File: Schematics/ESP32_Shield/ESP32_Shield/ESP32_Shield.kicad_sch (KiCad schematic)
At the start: 18 parts, among them J1 Conn_01x10, Q3 Si2319CDS, Q4 Si2319CDS, U6 ADS1234IPW, U7 SHT30-DIS

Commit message: kek
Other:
- note added: "-Verzerrung Spannungsteiler durch ADC Innenwiderstanding -> Widerstand verkleinen wenn nötig -Anti Aliasing -> Für DC? -Bestehende IC anschauen -> Nicht verfolgt. -wofür pullup -0.150s ladezeit überprüfen"
- note removed: "-Verzerrung Spannungsteiler durch ADC Innenwiderstanding -> Widerstand verkleinen wenn nötig -Anti Aliasing -> Für DC? -Bestehende IC anschauen -> Nicht verfolgt."
- moved on the sheet: Q4
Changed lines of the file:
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@@
 		)
 	)
-	(text "-Verzerrung Spannungsteiler durch ADC Innenwiderstanding -> Widerstand verkleinen wenn nötig\n-Anti Aliasing -> Für DC?\n-Bestehende IC anschauen -> Nicht verfolgt.\n\n"
+	(text "-Verzerrung Spannungsteiler durch ADC Innenwiderstanding -> Widerstand verkleinen wenn nötig\n-Anti Aliasing -> Für DC?\n-Bestehende IC anschauen -> Nicht verfolgt.\n-wofür pullup\n-0.150s ladezeit überprüfen\n\n"
 		(exclude_from_sim no)
 		(at 17.018 187.198 0)
@@
 	)
 	(junction
-		(at 209.55 140.97)
-		(diameter 0)
-		(color 0 0 0 0)
-	)
-	(junction
 		(at 234.95 149.86)
 		(diameter 0)
@@
 	(wire
 		(pts
-			(xy 190.5 153.67) (xy 209.55 153.67)
-		)
-		(stroke
-			(width 0)
-			(type default)
-		)
-	)
-	(wire
-		(pts
 			(xy 210.82 134.62) (xy 217.17 134.62)
 		)
@@
 	(wire
 		(pts
+			(xy 200.66 73.66) (xy 200.66 81.28)
+		)
+		(stroke
+			(width 0)
+			(type default)
+		)
+	)
+	(wire
+		(pts
 			(xy 76.2 34.29) (xy 91.44 34.29)
 		)
@@
 	(wire
 		(pts
-			(xy 180.34 144.78) (xy 185.42 144.78)
+			(xy 189.865 69.215) (xy 189.865 68.58)
 		)
 		(stroke
@@
 	(wire
 		(pts
-			(xy 209.55 129.54) (xy 209.55 140.97)
-		)
-		(stroke
-			(width 0)
-			(type default)
-		)
-	)
-	(wire
-		(pts
 			(xy 26.67 165.1) (xy 29.21 165.1)
 		)
@@
 	(wire
 		(pts
-			(xy 209.55 140.97) (xy 209.55 153.67)
+			(xy 209.55 140.97) (xy 209.55 129.54)
 		)
 		(stroke
@@
 	(wire
 		(pts
-			(xy 185.42 144.78) (xy 185.42 146.05)
+			(xy 189.865 68.58) (xy 193.04 68.58)
 		)
 		(stroke
@@
 	(global_label "!EN_DMS"
 		(shape input)
-		(at 180.34 144.78 180)
+		(at 189.865 69.215 180)
 		(fields_autoplaced yes)
 		(effects
@@
 		)
 		(property "Intersheetrefs" "${INTERSHEET_REFS}"
-			(at 169.372 144.78 0)
+			(at 178.897 69.215 0)
 			(effects
 				(font
@@
 	(symbol
 		(lib_id "power:+3.3V")
-		(at 180.34 153.67 90)
-		(mirror x)
+		(at 200.66 63.5 0)
 		(unit 1)
 		(exclude_from_sim no)
@@
 		(dnp no)
 		(property "Reference" "#PWR046"
-			(at 184.15 153.67 0)
+			(at 200.66 67.31 0)
 			(effects
 				(font
@@
 		)
 		(property "Value" "+3.3V"
-			(at 175.26 153.67 90)
+			(at 200.66 58.42 90)
 			(effects
 				(font
@@
 		)
 		(property "Footprint" ""
-			(at 180.34 153.67 0)
+			(at 200.66 63.5 0)
 			(effects
 				(font
@@
 		)
 		(property "Datasheet" ""
-			(at 180.34 153.67 0)
+			(at 200.66 63.5 0)
 			(effects
 				(font
@@
 		)
 		(property "Description" "Power symbol creates a global label with name \"+3.3V\""
-			(at 180.34 153.67 0)
+			(at 200.66 63.5 0)
 			(effects
 				(font
@@
 	(symbol
 		(lib_id "Transistor_FET:Si2319CDS")
-		(at 185.42 151.13 270)
+		(at 198.12 68.58 0)
+		(mirror x)
 		(unit 1)
 		(exclude_from_sim no)
@@
 		(fields_autoplaced yes)
 		(property "Reference" "Q4"
-			(at 185.42 157.48 90)
+			(at 204.47 68.58 90)
 			(effects
 				(font
@@
 		)
 		(property "Value" "Si2319CDS"
-			(at 185.42 160.02 90)
+			(at 207.01 68.58 90)
 			(effects
 				(font
@@
 		)
 		(property "Footprint" "Package_TO_SOT_SMD:SOT-23"
-			(at 183.515 156.21 0)
+			(at 203.2 66.675 0)
 			(effects
 				(font
@@
 		)
 		(property "Datasheet" "http://www.vishay.com/docs/66709/si2319cd.pdf"
-			(at 181.61 156.21 0)
+			(at 203.2 64.77 0)
 			(effects
 				(font
@@
 		)
 		(property "Description" "-4.4A Id, -40V Vds, P-Channel MOSFET, SOT-23"
-			(at 185.42 151.13 0)
-			(effects
-				(font
+			(at 198.12 68.58 0)
+			(effects
+				(font

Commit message: Order ready
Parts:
- added R22: 100k, Resistor_SMD:R_0603_1608Metric_Pad0.98x0.95mm_HandSolder, symbol Device:R
- R14, R15: value 510k -> 100k
- R21: value 10k -> 100k
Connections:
- net !EN_DMS: now also R22.1
- net +3.3V: now also R22.2
- net +BATT: now also Q3.2 (S); no longer Q3.3 (D)
- net -BATT: now also C14.1, R15.1
- net GND: no longer C14.1, R15.1
- net SCLK: no longer U2.24 (IO18)
- net at R14.1: now also Q3.3 (D); no longer Q3.2 (S)

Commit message: korrekturen
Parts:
- removed Q3: Si2319CDS, Package_TO_SOT_SMD:SOT-23, symbol Transistor_FET:Si2319CDS
- removed R21: 100k, Resistor_SMD:R_0603_1608Metric_Pad0.98x0.95mm_HandSolder, symbol Device:R
- added C1: 0.1u, Capacitor_SMD:C_0603_1608Metric_Pad1.08x0.95mm_HandSolder, symbol Device:C
- added Q1: Si1308EDL, Package_TO_SOT_SMD:SOT-323_SC-70, symbol Transistor_FET:Si1308EDL
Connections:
- net +3.3V: now also C1.2
- net +BATT: now also BAT_VOLT1.1 (Pin_1), R14.1; no longer BAT_VOLT1.2 (Pin_2)
- net GND: now also BAT_VOLT1.2 (Pin_2), C14.1, C1.1, Q1.2 (S)
- net bat_adc: no longer C14.2
- net !en_meas renamed en_meas
- net en_meas: now also C14.2, Q1.1 (G)
- removed net -BATT: BAT_VOLT1.1 (Pin_1), C14.1, R15.1
- new net: Q1.3 (D), R15.1
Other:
- moved on the sheet: BAT_VOLT1, C14, R14, R15

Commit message: ...
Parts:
- added PWR_ESP1, PWR_ESP2, PWR_ESP3, PWR_ESP32: Conn_01x02, Connector_PinHeader_2.54mm:PinHeader_1x02_P2.54mm_Vertical, symbol Connector_Generic:Conn_01x02
- added Q3: Si2319CDS, Package_TO_SOT_SMD:SOT-23, symbol Transistor_FET:Si2319CDS
- added R21: 100k, Resistor_SMD:R_0603_1608Metric_Pad0.98x0.95mm_HandSolder, symbol Device:R
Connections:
- net +3.3V: now also PWR_ESP2.1 (Pin_1), PWR_ESP3.1 (Pin_1); no longer C1.2, Q4.2 (S), R22.2, U6.1 (DVDD), U6.23 (GAIN0), U6.24 (GAIN1)
- net +5V: now also PWR_ESP32.1 (Pin_1); no longer U2.15 (5V)
- net +BATT: now also Q3.2 (S), R21.2; no longer R14.1
- net GND: now also R15.1
- net bat_adc: now also C14.2
- net en_meas: no longer C14.2
- net at Q1.3 (D): now also Q3.1 (G), R21.1; no longer R15.1
- new net: C1.2, PWR_ESP2.2 (Pin_2), U6.1 (DVDD), U6.23 (GAIN0), U6.24 (GAIN1)
- new net: PWR_ESP3.2 (Pin_2), Q4.2 (S), R22.2
- new net: Q3.3 (D), R14.1
- new net: PWR_ESP32.2 (Pin_2), U2.15 (5V)
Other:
- note added: "ESP32 Power In 5V über LDO innefizient Plan A. Buck converter 3.3, geht das? plan B: LDO, oder sogar dual mit LDO/Boost über jumper"
- moved on the sheet: C14, Q1, R14, R15

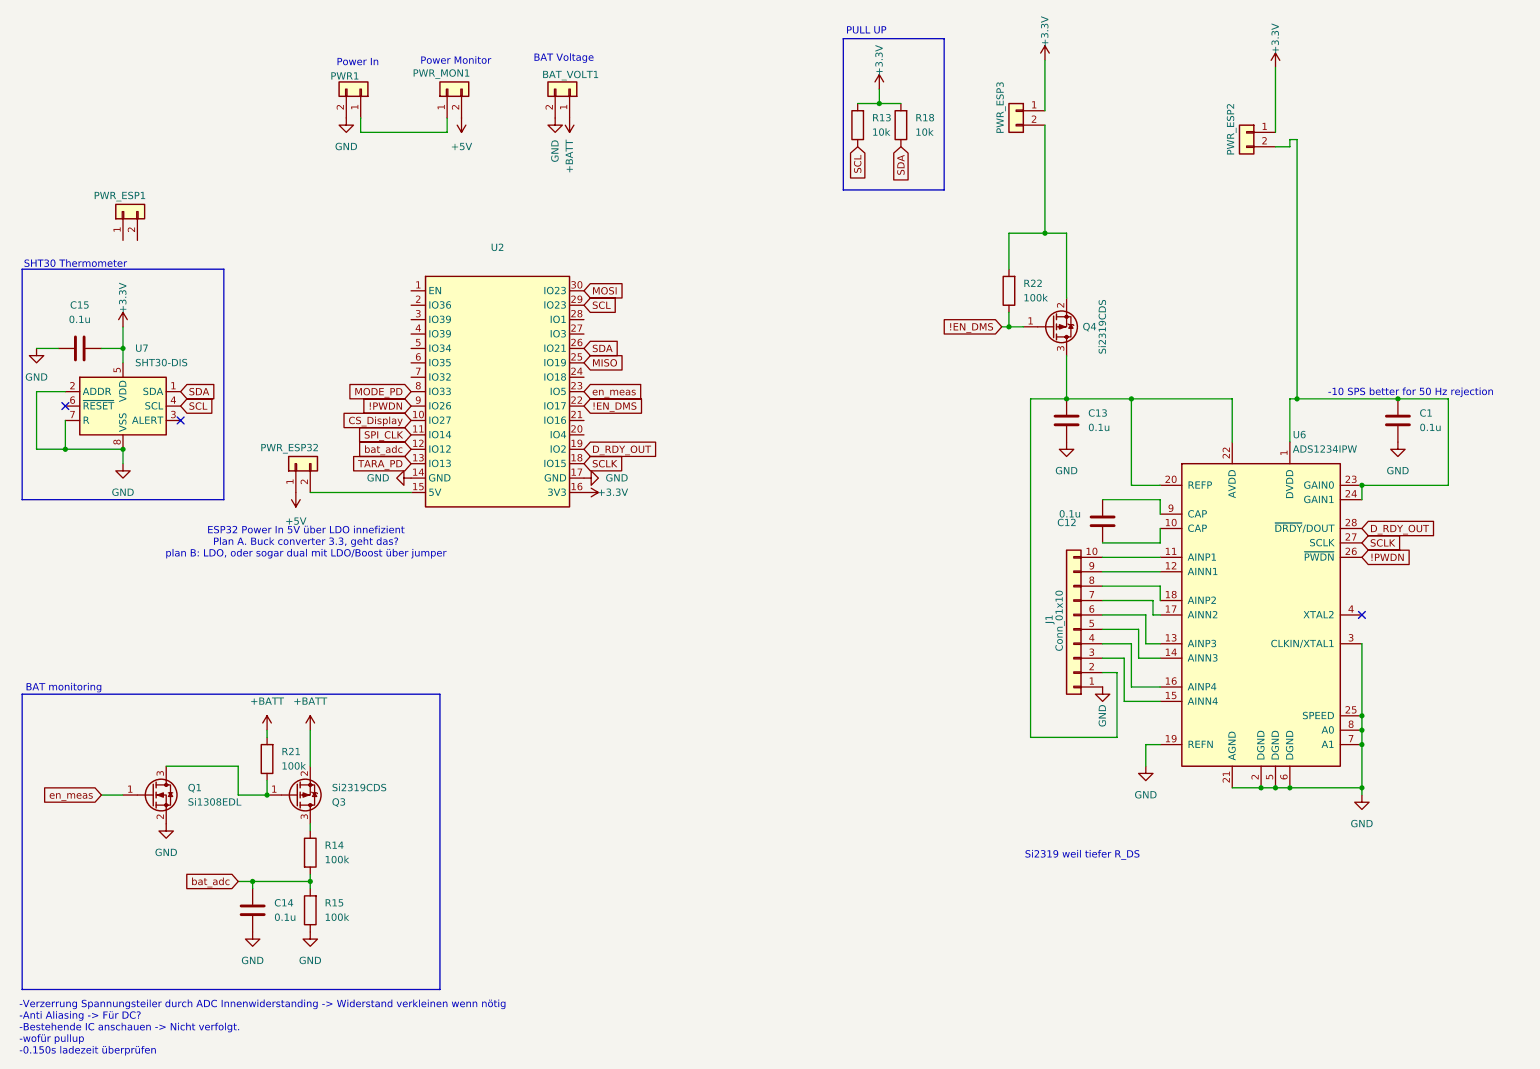
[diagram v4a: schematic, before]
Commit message: updated battery voltage monitor mosfet schematics
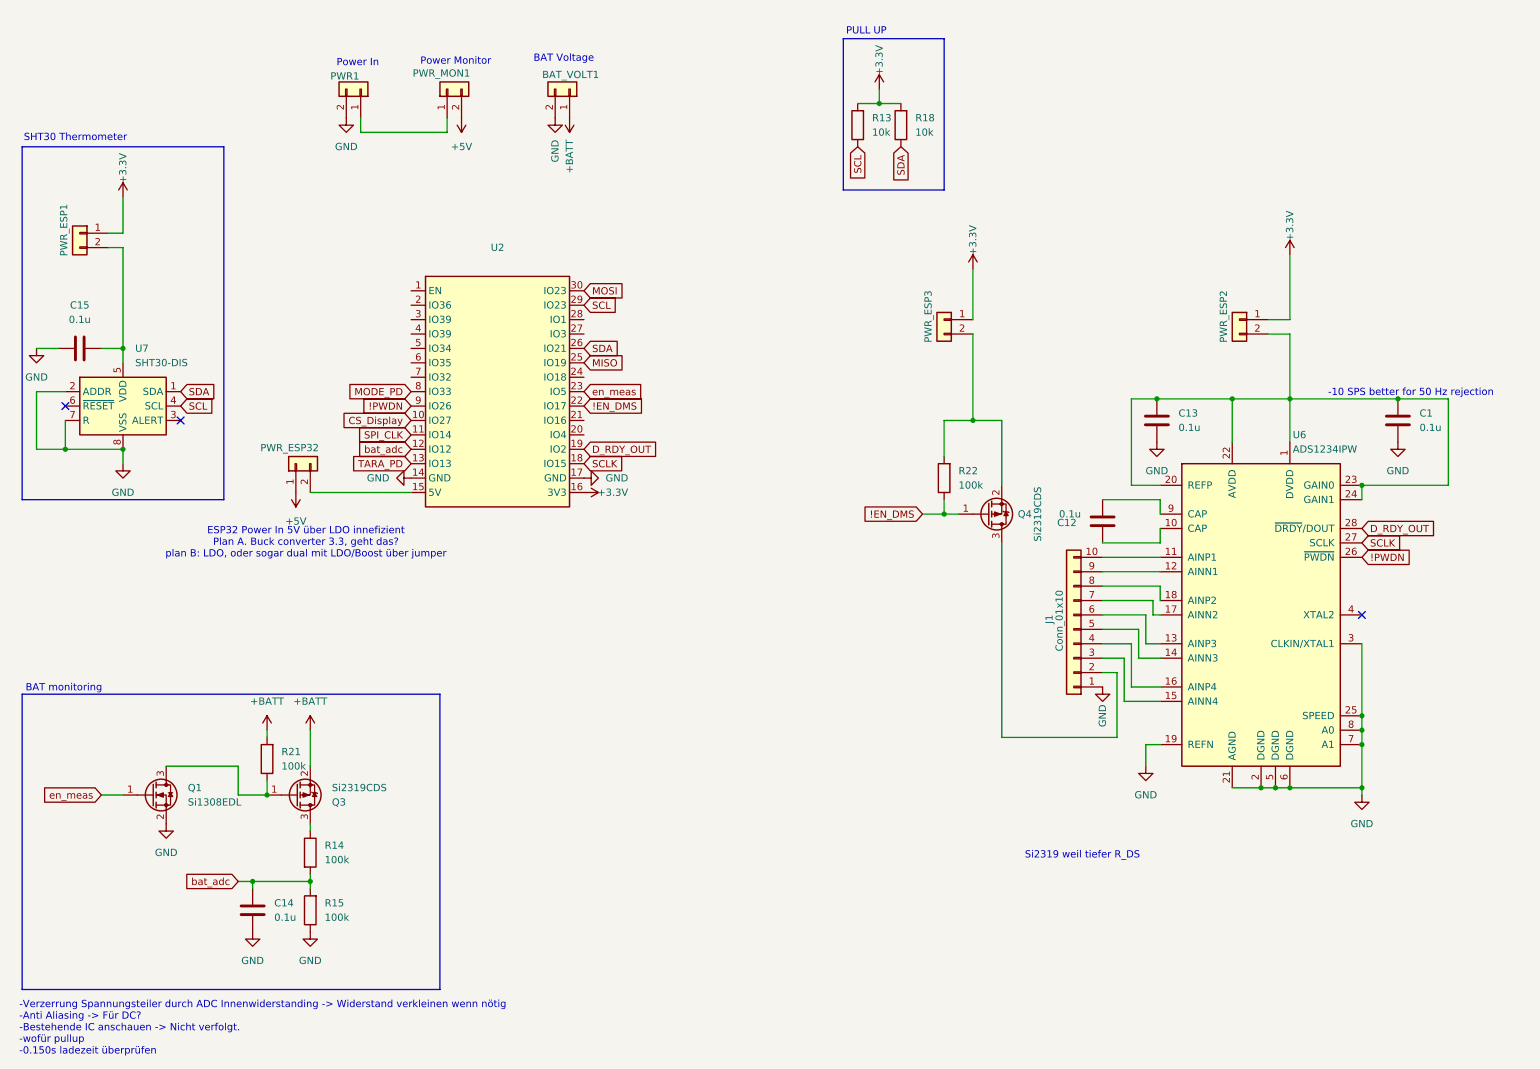
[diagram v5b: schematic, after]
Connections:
- net +3.3V: now also PWR_ESP1.1 (Pin_1); no longer C15.1, U7.5 (VDD)
- net at C1.2, PWR_ESP2.2 (Pin_2), U6.1 (DVDD)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: now also C13.2, U6.20 (REFP), U6.22 (AVDD)
- net at PWR_ESP1.2 (Pin_2): now also C15.1, U7.5 (VDD)
- new net: J1.2 (Pin_2), Q4.3 (D)
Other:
- moved on the sheet: C13, PWR_ESP1, PWR_ESP2, PWR_ESP3, Q4, R22

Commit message: Feedback umetzen
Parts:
- Q1: footprint Package_TO_SOT_SMD:SOT-323_SC-70 -> Package_TO_SOT_SMD:SOT-23
- renumbered PWR_ESP2 to ADC1, BAT_VOLT1 to BAT1, PWR_ESP3 to DMS1, PWR_ESP32 to ESP32, PWR_MON1 to PWR1, PWR_ESP1 to THRM1, PWR1 to V_IN1
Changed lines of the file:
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@@
 		(on_board yes)
 		(dnp no)
-		(property "Reference" "PWR_ESP32"
+		(property "Reference" "ESP32"
 			(at 68.834 89.916 90)
 			(effects
@@
 			(project "ESP32_Shield"
 				(path "/c333fcdd-d440-492d-a150-3b6c46d7ec2c"
-					(reference "PWR_ESP32")
+					(reference "ESP32")
 					(unit 1)
 				)
@@
 		(on_board yes)
 		(dnp no)
-		(property "Reference" "PWR_ESP3"
+		(property "Reference" "DMS1"
 			(at 176.276 71.374 90)
 			(effects
@@
 			(project "ESP32_Shield"
 				(path "/c333fcdd-d440-492d-a150-3b6c46d7ec2c"
-					(reference "PWR_ESP3")
+					(reference "DMS1")
 					(unit 1)
 				)
@@
 		(on_board yes)
 		(dnp no)
-		(property "Reference" "PWR_ESP1"
+		(property "Reference" "THRM1"
 			(at 23.876 56.134 90)
 			(effects
@@
 			(project "ESP32_Shield"
 				(path "/c333fcdd-d440-492d-a150-3b6c46d7ec2c"
-					(reference "PWR_ESP1")
+					(reference "THRM1")
 					(unit 1)
 				)
@@
 		(on_board yes)
 		(dnp no)
-		(property "Reference" "PWR1"
+		(property "Reference" "V_IN1"
 			(at 75.946 24.384 90)
 			(effects
@@
 			(project "ESP32_Shield"
 				(path "/c333fcdd-d440-492d-a150-3b6c46d7ec2c"
-					(reference "PWR1")
+					(reference "V_IN1")
 					(unit 1)
 				)
@@
 			)
 		)
-		(property "Footprint" "Package_TO_SOT_SMD:SOT-323_SC-70"
+		(property "Footprint" "Package_TO_SOT_SMD:SOT-23"
 			(at 44.45 153.035 0)
 			(effects
@@
 		(on_board yes)
 		(dnp no)
-		(property "Reference" "PWR_MON1"
-			(at 95.504 23.876 90)
+		(property "Reference" "PWR1"
+			(at 93.98 23.876 90)
 			(effects
 				(font
@@
 			(project "ESP32_Shield"
 				(path "/c333fcdd-d440-492d-a150-3b6c46d7ec2c"
-					(reference "PWR_MON1")
+					(reference "PWR1")
 					(unit 1)
 				)
@@
 		(on_board yes)
 		(dnp no)
-		(property "Reference" "PWR_ESP2"
+		(property "Reference" "ADC1"
 			(at 228.346 71.374 90)
 			(effects
@@
 			(project "ESP32_Shield"
 				(path "/c333fcdd-d440-492d-a150-3b6c46d7ec2c"
-					(reference "PWR_ESP2")
+					(reference "ADC1")
 					(unit 1)
 				)
@@
 		(on_board yes)
 		(dnp no)
-		(property "Reference" "BAT_VOLT1"
+		(property "Reference" "BAT1"
 			(at 108.204 24.13 90)
 			(effects
@@
 			(project "ESP32_Shield"
 				(path "/c333fcdd-d440-492d-a150-3b6c46d7ec2c"
-					(reference "BAT_VOLT1")
-					(unit 1)
-				)
+					(reference "BAT1")
+					(unit 1)
+				)

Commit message: a
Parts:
- added C6: 10u, Capacitor_SMD:C_0603_1608Metric_Pad1.08x0.95mm_HandSolder, symbol Device:C
- added C7: 22u, Capacitor_SMD:C_0603_1608Metric_Pad1.08x0.95mm_HandSolder, symbol Device:C
- added ESP3.3V1: Conn_01x02, Connector_PinHeader_2.54mm:PinHeader_1x02_P2.54mm_Vertical, symbol Connector_Generic:Conn_01x02
- added L1: 0.47u, Inductor_SMD:L_Coilcraft_XxL4020, symbol Device:L
- added R8: 511k, Resistor_SMD:R_0603_1608Metric_Pad0.98x0.95mm_HandSolder, symbol Device:R
- added R9: 91k, Resistor_SMD:R_0603_1608Metric_Pad0.98x0.95mm_HandSolder, symbol Device:R
- added S1: JS202011SCQN, Button_Switch_SMD:SW_DPDT_CK_JS202011JCQN, symbol JS202011SCQN:JS202011SCQN
- added U4: TPS63802DLAR, TPS63802DLAR:VREG_TPS63802DLAR, symbol TPS63802DLAR:TPS63802DLAR
- renumbered V_IN1 to 6V_IN1, ESP32 to ESP5V1
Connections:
- net +3.3V: now also C7.2, ESP3.3V1.1 (Pin_1), R8.1, U4.6 (VOUT); no longer U2.16 (3V3)
- net +5V: now also S1.2; no longer ESP5V1.1 (Pin_1)
- net GND: now also C6.2, C7.1, R9.2, U4.2 (MODE), U4.3 (AGND), U4.8 (GND)
- new net: R8.2, R9.1, U4.4 (FB)
- new net: L1.2, U4.7 (L2)
- new net: L1.1, U4.9 (L1)
- new net: ESP3.3V1.2 (Pin_2), U2.16 (3V3)
- new net 5V BUCK: C6.1, S1.3, U4.1 (EN), U4.10 (VIN)
- new net 5V LDO: ESP5V1.1 (Pin_1), S1.1
- no-connect marks 3 -> 4
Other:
- moved on the sheet: ESP5V1

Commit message: l
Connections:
- net SCL: no longer U2.29 (IO23)
- net A0: now reaches U2.20 (IO4)
- net BSY_ePAP: now reaches U2.21 (IO16)
- net A1: now reaches U2.7 (IO32)
- net CS_Display renamed CS_ePAP
- net MISO renamed RST_ePAP
